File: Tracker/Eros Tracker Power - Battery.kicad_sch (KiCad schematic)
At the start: 17 parts, among them Q4 DMP2240UDM-7, Q5 DMC1028UVT-7, Q6 DMC1028UVT-7, U2 TPS62A01A, U3 MCP73834-FCI/MF

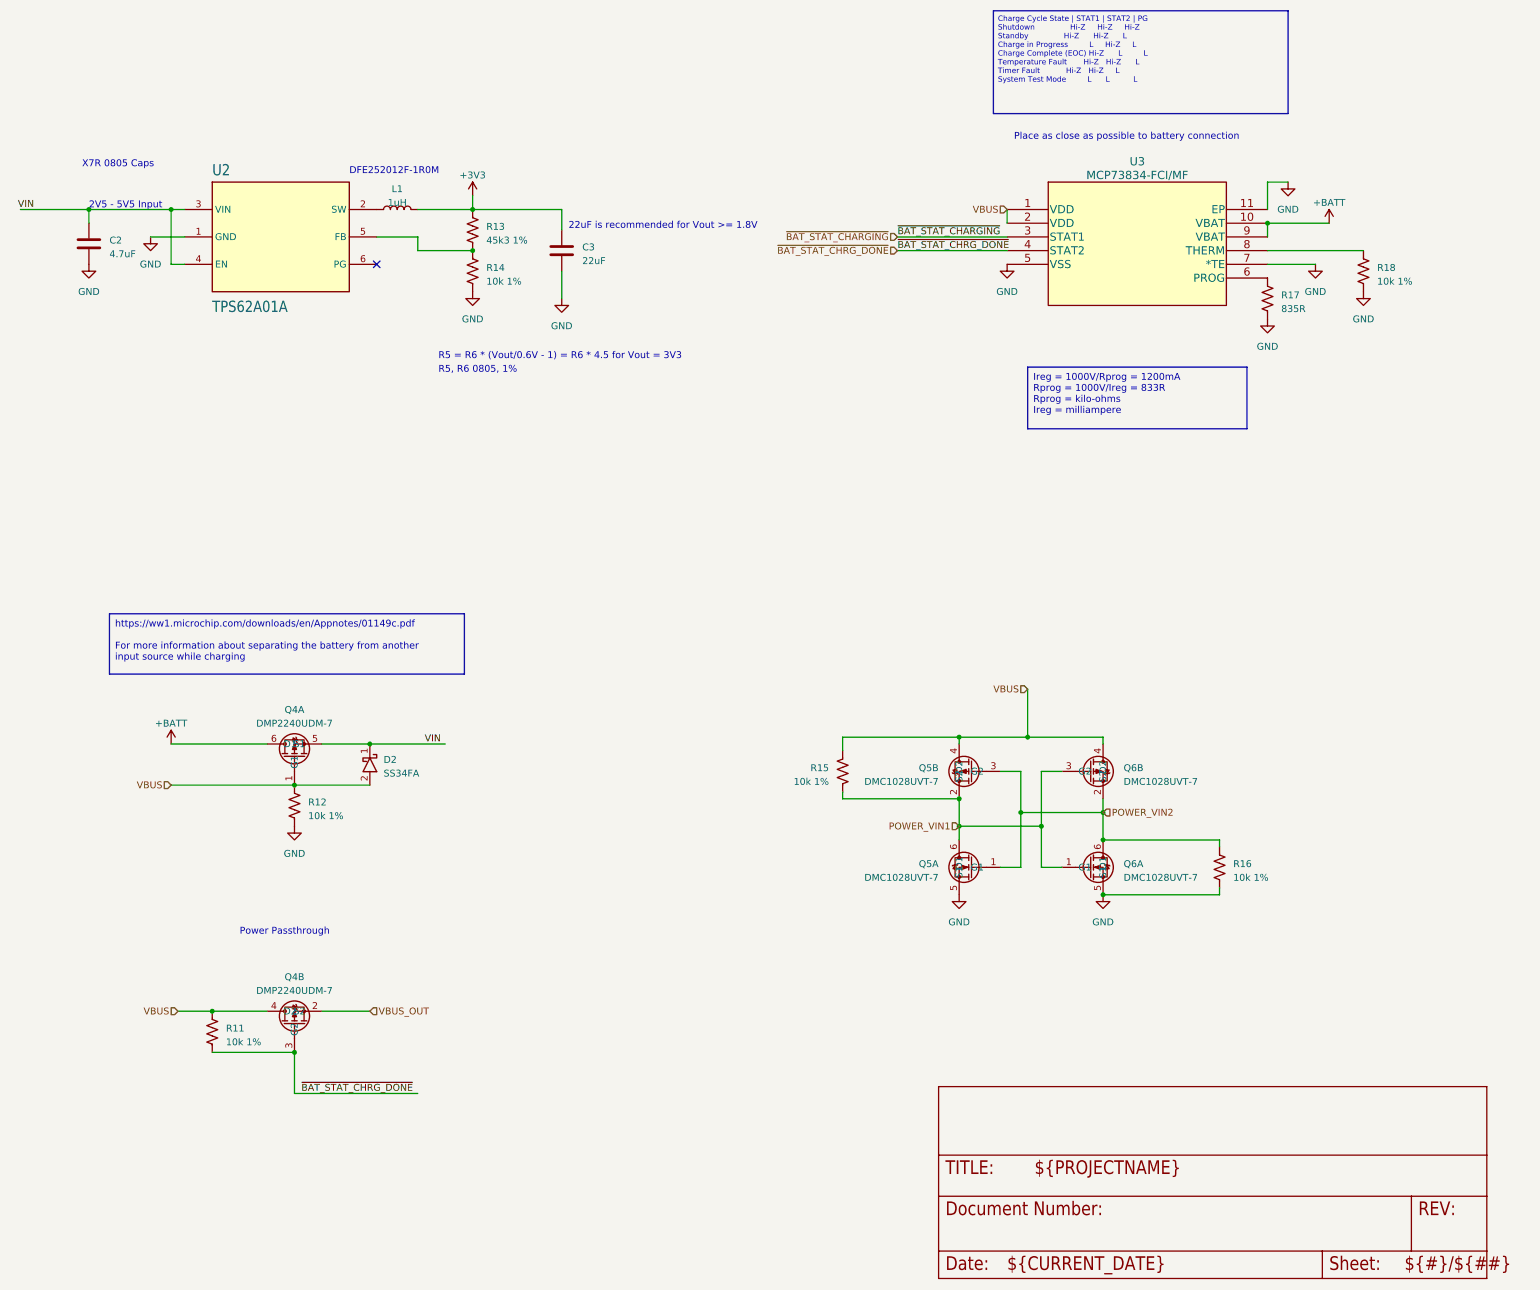
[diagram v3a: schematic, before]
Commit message: RevC release. Power passthrough, battery voltage monitoring, IMU interrupt line fixed. TVS diodes added to all human-reachable connections.
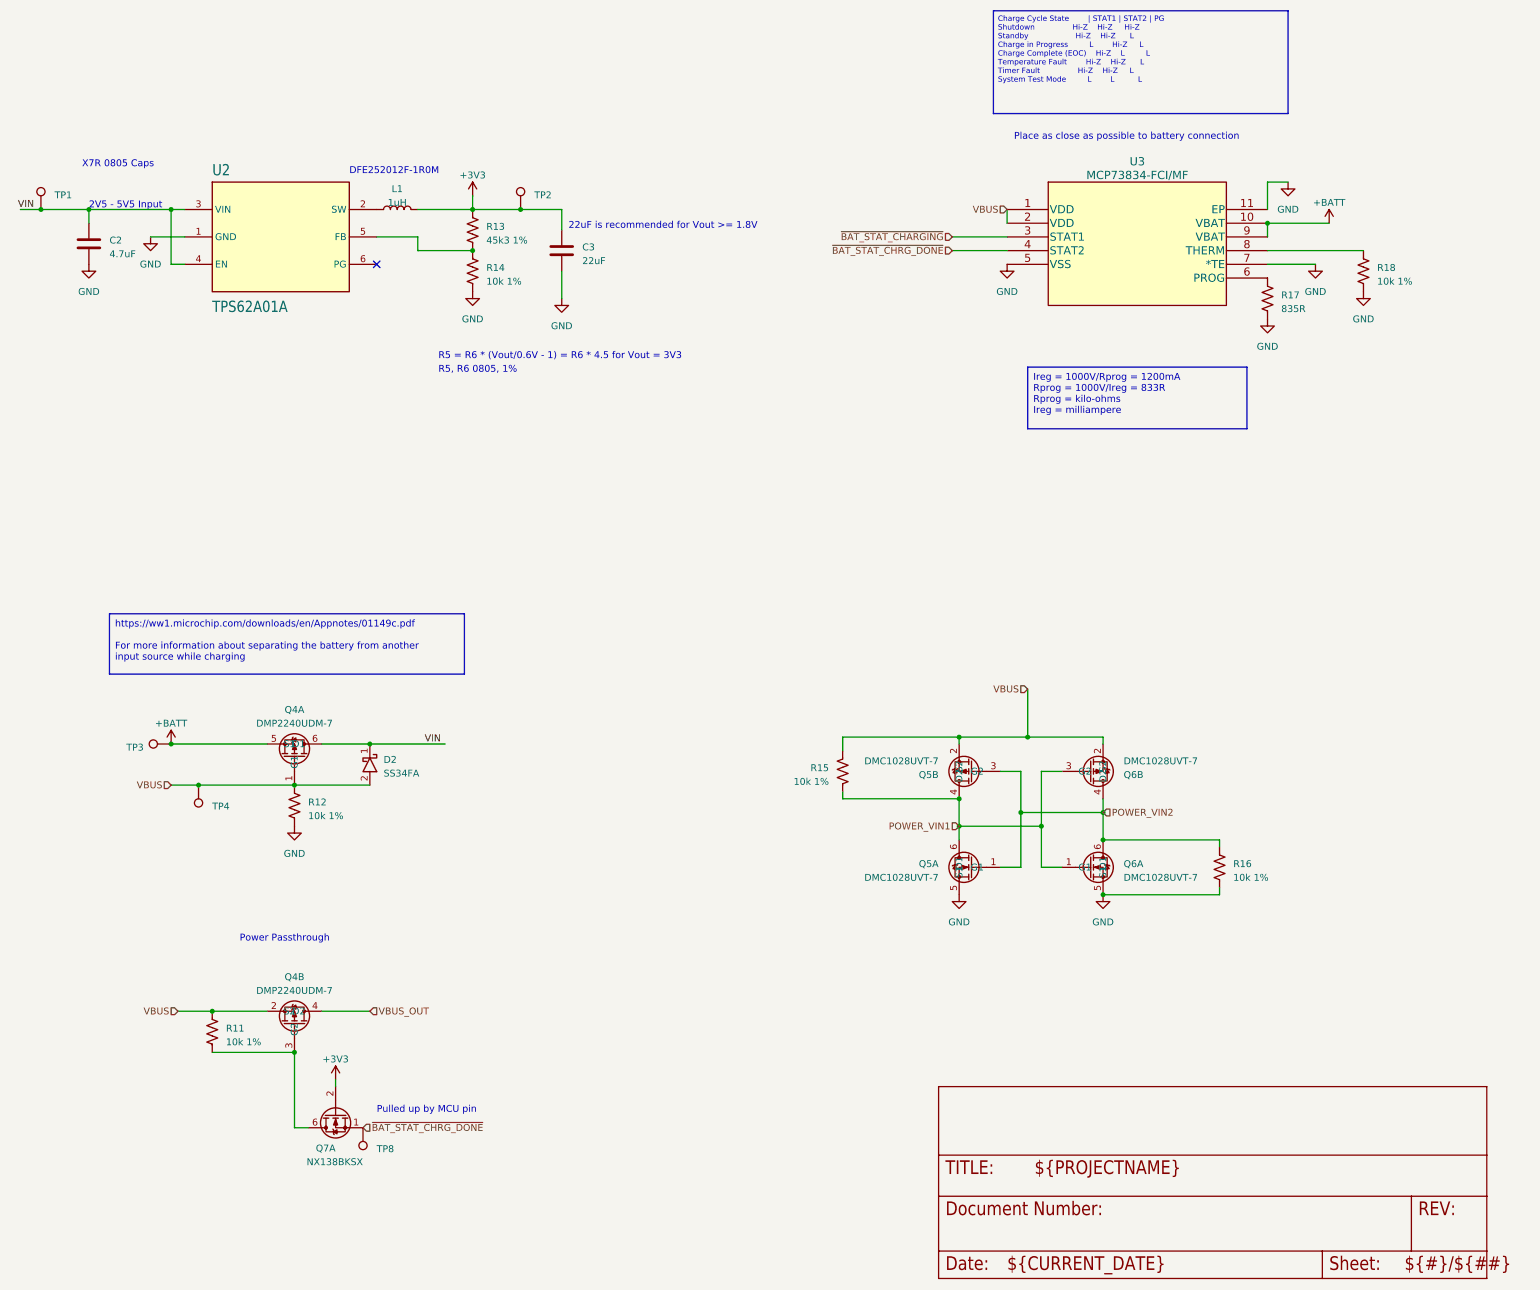
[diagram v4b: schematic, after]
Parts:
- added Q7: NX138BKSX, Eros Tracker:SOT65P210X110-6N, symbol Eros Tracker:NX138BKSX
- added TP1, TP2, TP3, TP4, TP8: TestPoint, TestPoint:TestPoint_Pad_D1.0mm, symbol Connector:TestPoint
- D2: footprint SODFL3618X143N -> Eros Tracker:SODFL3618X143N
- Q4: footprint SOT95P285X140-6N -> Eros Tracker:SOT95P285X140-6N
- Q5, Q6: footprint SOT95P280X100-6N -> Eros Tracker:SOT95P285X140-6N
- R11, R12, R14, R15, R16, R18: footprint Resistor_SMD:R_0805_2012Metric -> Resistor_SMD:R_0402_1005Metric; Manufacturer_Part_Number RT0805FRE0710KL -> RT0402FRE0710KL; Mouser Part Number 603-RT0805FRE0710KL -> 603-RT0402FRE0710KL; Mouser Price/Stock https://www.mouser.com/ProductDetail/YAGEO/RT0805FRE0710KL?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 -> https://www.mouser.com/ProductDetail/YAGEO/RT0402FRE0710KL?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
- R13: footprint Resistor_SMD:R_0805_2012Metric -> Resistor_SMD:R_0402_1005Metric; Manufacturer_Name YAGEO -> Susumu; Manufacturer_Part_Number RT0805DRE0745K3L -> RR0510P-4532-D; Mouser Part Number 603-RT0805DRE0745K3L -> 754-RR0510P-4532D; Mouser Price/Stock https://www.mouser.com/ProductDetail/YAGEO/RT0805DRE0745K3L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 -> https://www.mouser.com/ProductDetail/Susumu/RR0510P-4532-D?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
- U2: footprint Eros Tracker:SOT-563 -> Eros Tracker:TPS62A0xA-SOT-563
- U3: footprint DFN10_3x3MC_MCH -> Eros Tracker:MCP73834-FCI-MF
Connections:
- net +3V3: now also Q7.2 (G1), TP2.1
- net +BATT: now also Q4.5 (S1), TP3.1; no longer Q4.6 (D1)
- net POWER_VIN1: now also Q5.4 (D2); no longer Q5.2 (S2)
- net POWER_VIN2: now also Q6.4 (D2); no longer Q6.2 (S2)
- net VBUS: now also Q4.2 (S2), Q5.2 (S2), Q6.2 (S2), TP4.1; no longer Q4.4 (D2), Q5.4 (D2), Q6.4 (D2)
- net VBUS_OUT: now also Q4.4 (D2); no longer Q4.2 (S2)
- net VIN: now also Q4.6 (D1), TP1.1; no longer Q4.5 (S1)
- net ~{BAT_STAT_CHRG_DONE}: now also Q7.1 (S1), TP8.1; no longer Q4.3 (G2), R11.2
- new net: Q4.3 (G2), Q7.6 (D1), R11.2
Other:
- note added: "Pulled up by MCU pin"
- moved on the sheet: Q4A, Q4B, Q5B
